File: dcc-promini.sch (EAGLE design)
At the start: 7 parts, among them Q1 MOSFET-NCHANNEL2N7002PW

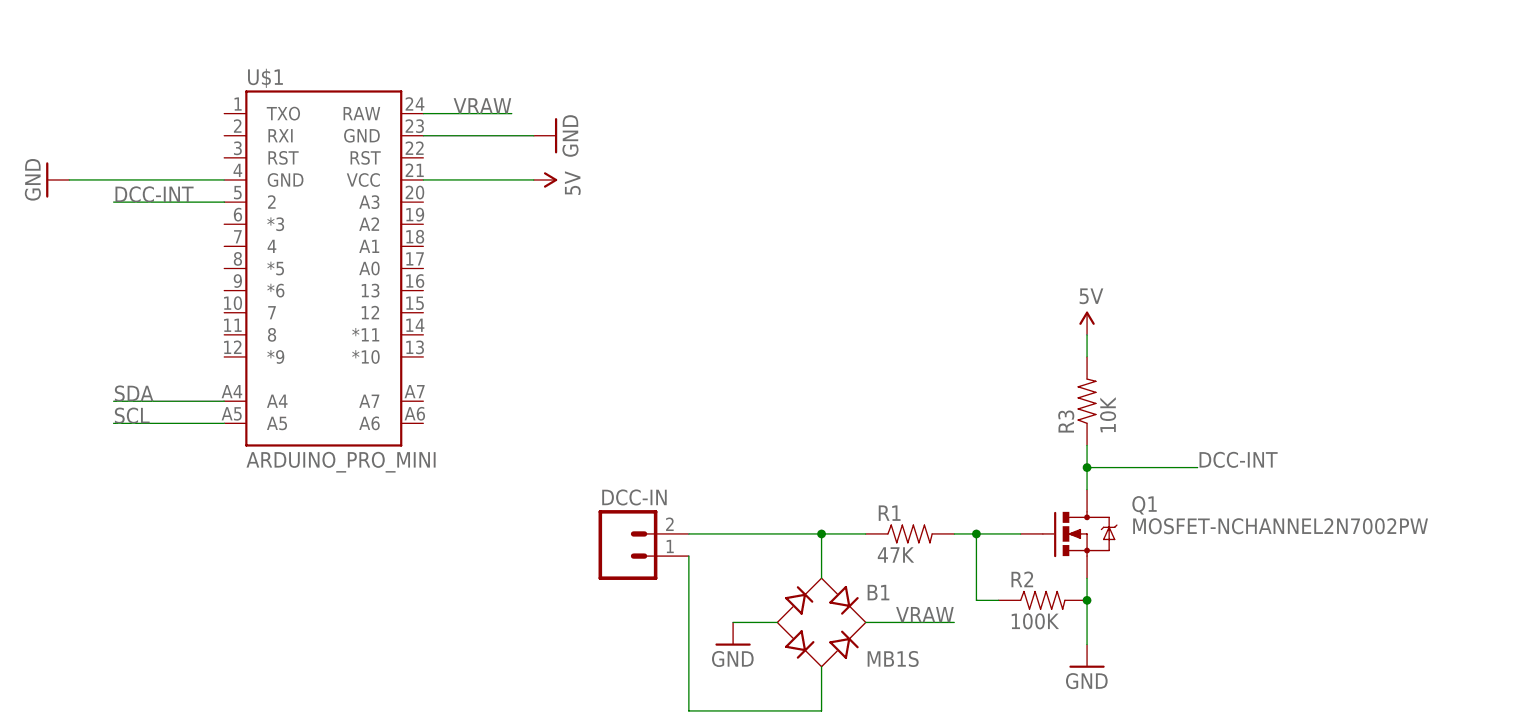
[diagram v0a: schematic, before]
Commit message: add a-star variant, use JST for dcc-powered boards
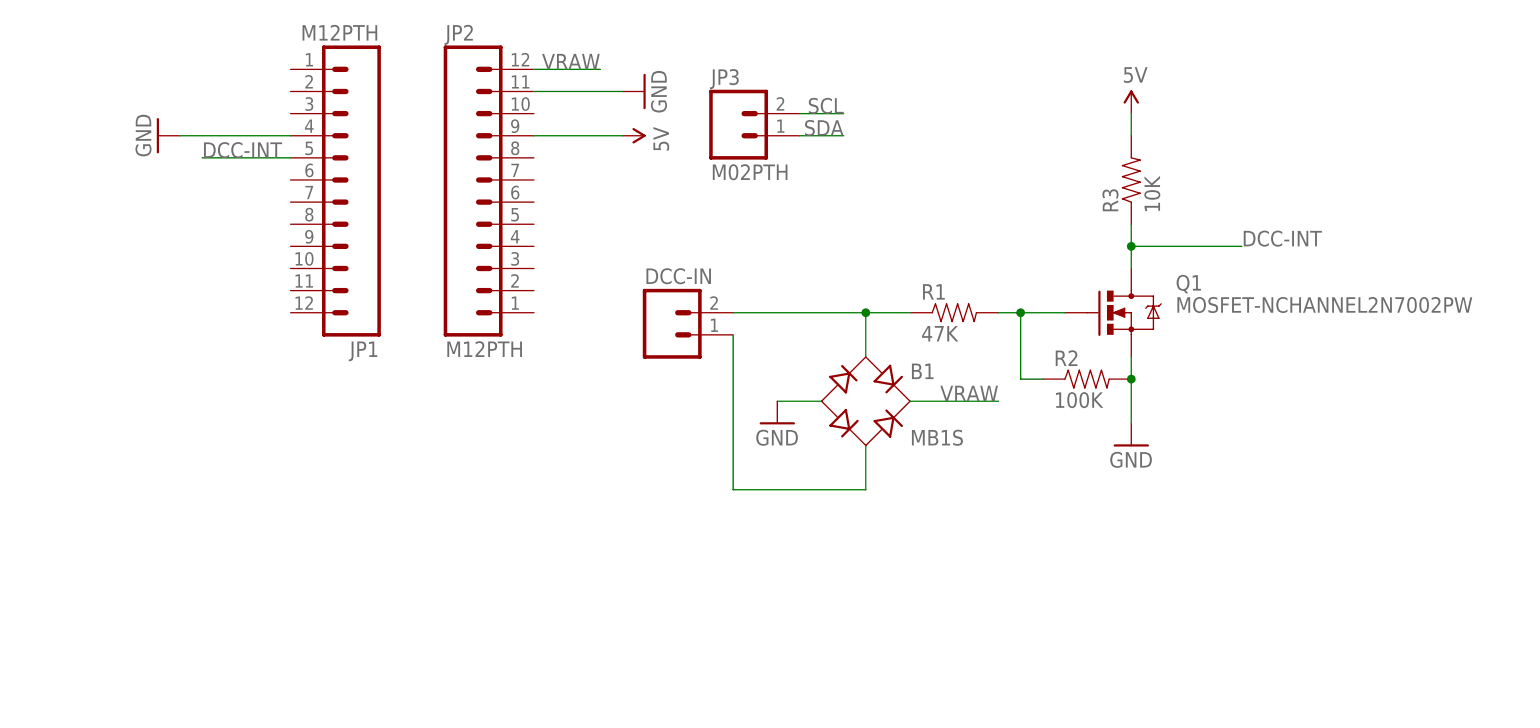
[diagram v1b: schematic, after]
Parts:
- removed U$1: ARDUINO_PRO_MINI, SparkFun-Boards:ARDUINO_PRO_MINI
- added JP1, JP2: M12PTH, SparkFun-Connectors:M12PTH
- added JP3: M02PTH, SparkFun-Connectors:M02PTH
- DCC-IN: value M02PTH -> M02-JST-2-PTH-NO_SILK; device SparkFun-Connectors:M02PTH -> SparkFun-Connectors:M02-JST-2-PTH-NO_SILK
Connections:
- net 5V: now also JP2.9; no longer U$1.VCC
- net DCC-INT: now also JP1.5; no longer U$1.2
- net GND: now also JP1.4, JP2.11; no longer U$1.GND, U$1.GND@2
- net SCL: now also JP3.2; no longer U$1.A5
- net SDA: now also JP3.1; no longer U$1.A4
- net VRAW: now also JP2.12; no longer U$1.RAW
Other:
- moved on the sheet: B1, DCC-IN, Q1, R1, R2, R3
